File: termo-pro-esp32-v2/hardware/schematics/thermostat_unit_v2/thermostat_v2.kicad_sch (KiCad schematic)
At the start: 22 parts, among them J1 Conn_01x08_Pin, Q1 PN2222A, Q2 PN2222A, SW1 SW_Push, SW2 SW_Push, SW3 SW_Push, SW4 SW_Push, U1 NODEMCU-32S, U2 DHT11

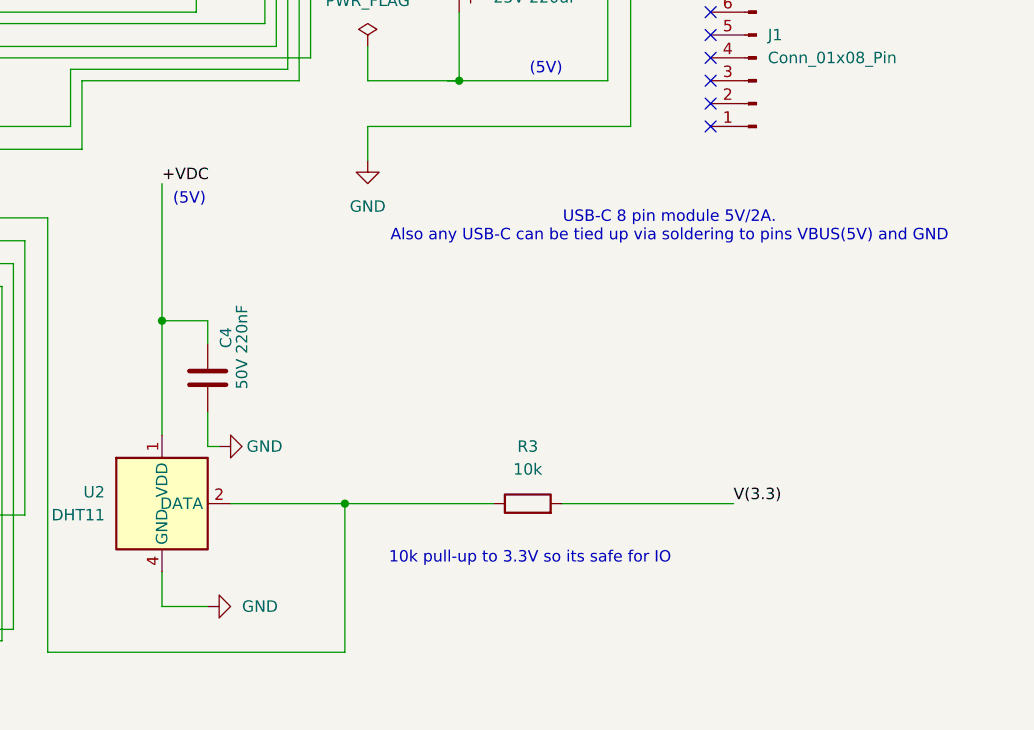
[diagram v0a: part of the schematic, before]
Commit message: minor thermostat pcb and schematic fix , missed to put the 3.3V net to DHT11, put the 5V instead, mistake
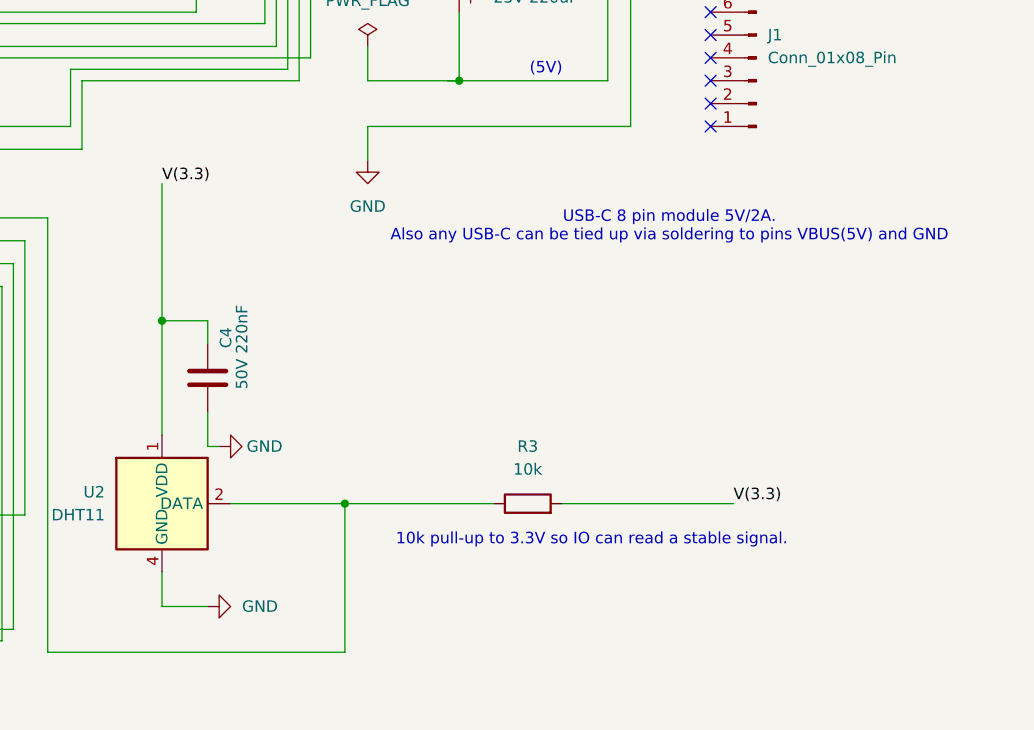
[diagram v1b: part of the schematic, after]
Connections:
- net +VDC: no longer C4.2, U2.1 (VDD)
- net V(3.3): now also C4.2, U2.1 (VDD)
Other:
- note added: "10k pull-up to 3.3V so IO can read a stable signal."
- note removed: "10k pull-up to 3.3V so its safe for IO"
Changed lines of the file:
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@@
 		)
 	)
-	(text "10k pull-up to 3.3V so its safe for IO"
+	(text "10k pull-up to 3.3V so IO can read a stable signal."
 		(exclude_from_sim no)
-		(at 227.584 152.146 0)
+		(at 234.442 150.114 0)
 		(effects
 			(font
@@
 	(text "(5V)"
 		(exclude_from_sim no)
-		(at 189.738 112.268 0)
-		(effects
-			(font
-				(size 1.27 1.27)
-				(color 0 0 0 1)
-			)
-		)
-	)
-	(text "(5V)"
-		(exclude_from_sim no)
 		(at 229.362 97.79 0)
 		(effects
@@
 		)
 	)
-	(label "+VDC"
-		(at 162.56 73.66 0)
+	(label "V(3.3)"
+		(at 186.69 110.49 0)
 		(effects
 			(font
 				(size 1.27 1.27)
+				(color 255 0 0 1)
 			)
 			(justify left bottom)
@@
 	)
 	(label "+VDC"
-		(at 241.3 88.9 0)
+		(at 162.56 73.66 0)
 		(effects
 			(font
@@
 		)
 	)
-	(label "V(3.3)"
-		(at 250.19 146.05 0)
+	(label "+VDC"
+		(at 241.3 88.9 0)
 		(effects
 			(font
 				(size 1.27 1.27)
-				(color 255 0 0 1)
 			)
 			(justify left bottom)
@@
 	)
 	(label "V(3.3)"
-		(at 166.37 78.74 0)
+		(at 250.19 146.05 0)
 		(effects
 			(font
@@
 		)
 	)
-	(label "+VDC"
-		(at 186.69 110.49 0)
+	(label "V(3.3)"
+		(at 166.37 78.74 0)
 		(effects
 			(font
 				(size 1.27 1.27)
+				(color 255 0 0 1)
 			)
 			(justify left bottom)
@@
 		)
 		(instances
-			(project "termostat-v2"
+			(project "thermostat_v2"
 				(path "/ac78e03d-eaa5-43c4-8730-cba06800c7fc"
 					(reference "#PWR010")
@@
 		)
 		(instances
-			(project "termostat-v2"
+			(project "thermostat_v2"
 				(path "/ac78e03d-eaa5-43c4-8730-cba06800c7fc"
 					(reference "#PWR017")
@@
 		)
 		(instances
-			(project "termostat-v2"
+			(project "thermostat_v2"
 				(path "/ac78e03d-eaa5-43c4-8730-cba06800c7fc"
 					(reference "J1")
@@
 		)
 		(instances
-			(project "termostat-v2"
+			(project "thermostat_v2"
 				(path "/ac78e03d-eaa5-43c4-8730-cba06800c7fc"
 					(reference "#PWR03")
@@
 		)
 		(instances
-			(project "termostat-v2"
+			(project "thermostat_v2"
 				(path "/ac78e03d-eaa5-43c4-8730-cba06800c7fc"
 					(reference "R7")
@@
 		)
 		(instances
-			(project "termostat-v2"
+			(project "thermostat_v2"
 				(path "/ac78e03d-eaa5-43c4-8730-cba06800c7fc"
 					(reference "#PWR018")
@@
 		)
 		(instances
-			(project "termostat-v2"
+			(project "thermostat_v2"
 				(path "/ac78e03d-eaa5-43c4-8730-cba06800c7fc"
 					(reference "#FLG04")
@@
 		)
 		(instances
-			(project "termostat-v2"
+			(project "thermostat_v2"
 				(path "/ac78e03d-eaa5-43c4-8730-cba06800c7fc"
 					(reference "#PWR09")
@@
 		)
 		(instances
-			(project "termostat-v2"
+			(project "thermostat_v2"
 				(path "/ac78e03d-eaa5-43c4-8730-cba06800c7fc"
 					(reference "R4")
@@
 		)
 		(instances
-			(project "termostat-v2"
+			(project "thermostat_v2"
 				(path "/ac78e03d-eaa5-43c4-8730-cba06800c7fc"
 					(reference "C2")
@@
 		)
 		(instances
-			(project "termostat-v2"
+			(project "thermostat_v2"
 				(path "/ac78e03d-eaa5-43c4-8730-cba06800c7fc"
 					(reference "#PWR07")
@@
 		)
 		(instances
-			(project "termostat-v2"
+			(project "thermostat_v2"
 				(path "/ac78e03d-eaa5-43c4-8730-cba06800c7fc"
 					(reference "SW1")
@@
 		)
 		(instances
-			(project "termostat-v2"
+			(project "thermostat_v2"
 				(path "/ac78e03d-eaa5-43c4-8730-cba06800c7fc"
 					(reference "Q1")
@@
 		)
 		(instances
-			(project "termostat-v2"
+			(project "thermostat_v2"
 				(path "/ac78e03d-eaa5-43c4-8730-cba06800c7fc"
 					(reference "C1")
@@
 		)
 		(instances
-			(project "termostat-v2"
+			(project "thermostat_v2"
 				(path "/ac78e03d-eaa5-43c4-8730-cba06800c7fc"
 					(reference "#FLG01")
@@
 		)
 		(instances
-			(project "termostat-v2"
+			(project "thermostat_v2"
 				(path "/ac78e03d-eaa5-43c4-8730-cba06800c7fc"
 					(reference "C3")
@@
 		)
 		(instances
-			(project "termostat-v2"
+			(project "thermostat_v2"
 				(path "/ac78e03d-eaa5-43c4-8730-cba06800c7fc"
 					(reference "U2")
@@
 		)
 		(instances
-			(project "termostat-v2"
+			(project "thermostat_v2"
 				(path "/ac78e03d-eaa5-43c4-8730-cba06800c7fc"
 					(reference "U1")
@@
 		)
 		(instances
-			(project "termostat-v2"
+			(project "thermostat_v2"
 				(path "/ac78e03d-eaa5-43c4-8730-cba06800c7fc"
 					(reference "#FLG03")
@@
 		)
 		(instances
-			(project "termostat-v2"
+			(project "thermostat_v2"
 				(path "/ac78e03d-eaa5-43c4-8730-cba06800c7fc"
 					(reference "SW2")
@@
 		)
 		(instances
-			(project "termostat-v2"
+			(project "thermostat_v2"
 				(path "/ac78e03d-eaa5-43c4-8730-cba06800c7fc"
 					(reference "#PWR02")
@@
 		)
 		(instances
-			(project "termostat-v2"
+			(project "thermostat_v2"
 				(path "/ac78e03d-eaa5-43c4-8730-cba06800c7fc"
 					(reference "#PWR08")
@@
 		)
 		(instances
-			(project "termostat-v2"
+			(project "thermostat_v2"
 				(path "/ac78e03d-eaa5-43c4-8730-cba06800c7fc"
 					(reference "#PWR01")
@@
 		)
 		(instances
-			(project "termostat-v2"
+			(project "thermostat_v2"
 				(path "/ac78e03d-eaa5-43c4-8730-cba06800c7fc"
 					(reference "BZ1")
@@
 		)
 		(instances
-			(project "termostat-v2"
+			(project "thermostat_v2"
 				(path "/ac78e03d-eaa5-43c4-8730-cba06800c7fc"
 					(reference "SW4")
@@
 		)
 		(instances
-			(project "termostat-v2"
+			(project "thermostat_v2"
 				(path "/ac78e03d-eaa5-43c4-8730-cba06800c7fc"
 					(reference "#PWR05")
@@
 		)
 		(instances
-			(project "termostat-v2"
+			(project "thermostat_v2"
 				(path "/ac78e03d-eaa5-43c4-8730-cba06800c7fc"
 					(reference "#PWR011")
@@
 		)
 		(instances
-			(project "termostat-v2"
+			(project "thermostat_v2"
 				(path "/ac78e03d-eaa5-43c4-8730-cba06800c7fc"
 					(reference "SW3")
@@
 		)
 		(instances
-			(project "termostat-v2"
+			(project "thermostat_v2"
 				(path "/ac78e03d-eaa5-43c4-8730-cba06800c7fc"
 					(reference "#PWR019")
@@
 		)
 		(instances
-			(project "termostat-v2"
+			(project "thermostat_v2"
 				(path "/ac78e03d-eaa5-43c4-8730-cba06800c7fc"
 					(reference "DS2")
@@
 		)
 		(instances
-			(project "termostat-v2"
+			(project "thermostat_v2"
 				(path "/ac78e03d-eaa5-43c4-8730-cba06800c7fc"
 					(reference "Q2")
@@
 		)
 		(instances
-			(project "termostat-v2"
+			(project "thermostat_v2"
 				(path "/ac78e03d-eaa5-43c4-8730-cba06800c7fc"
 					(reference "D1")
@@
 		)
 		(instances
-			(project "termostat-v2"
+			(project "thermostat_v2"
 				(path "/ac78e03d-eaa5-43c4-8730-cba06800c7fc"
 					(reference "R3")
@@
 		)
 		(instances
-			(project "termostat-v2"
+			(project "thermostat_v2"
 				(path "/ac78e03d-eaa5-43c4-8730-cba06800c7fc"
 					(reference "C4")
@@
 		)
 		(instances
-			(project "termostat-v2"
+			(project "thermostat_v2"
 				(path "/ac78e03d-eaa5-43c4-8730-cba06800c7fc"
 					(reference "#FLG05")
@@
 		)
 		(instances
-			(project "termostat-v2"
+			(project "thermostat_v2"
 				(path "/ac78e03d-eaa5-43c4-8730-cba06800c7fc"
 					(reference "#PWR04")
@@
 		)
 		(instances
-			(project "termostat-v2"
+			(project "thermostat_v2"
 				(path "/ac78e03d-eaa5-43c4-8730-cba06800c7fc"
 					(reference "R2")
@@
 		)
 		(instances
-			(project "termostat-v2"
+			(project "thermostat_v2"
 				(path "/ac78e03d-eaa5-43c4-8730-cba06800c7fc"
 					(reference "#PWR014")
@@
 		)
 		(instances
-			(project "termostat-v2"
+			(project "thermostat_v2"
 				(path "/ac78e03d-eaa5-43c4-8730-cba06800c7fc"
 					(reference "#PWR06")
@@
 		)
 		(instances
-			(project "termostat-v2"
+			(project "thermostat_v2"
 				(path "/ac78e03d-eaa5-43c4-8730-cba06800c7fc"
 					(reference "RV3")
@@
 		)
 		(instances
-			(project "termostat-v2"
+			(project "thermostat_v2"
 				(path "/ac78e03d-eaa5-43c4-8730-cba06800c7fc"
 					(reference "R1")
